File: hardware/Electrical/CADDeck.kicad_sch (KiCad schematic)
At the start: 26 parts, among them SW1 SW_Push, SW10 SW_Push, SW2 SW_Push, SW3 SW_Push, SW4 SW_Push, SW5 SW_Push, SW6 SW_Push, SW7 SW_Push, SW8 SW_Push, SW9 SW_Push, U4 49E Zoom, U5 49E Rotate, U6 TTP223

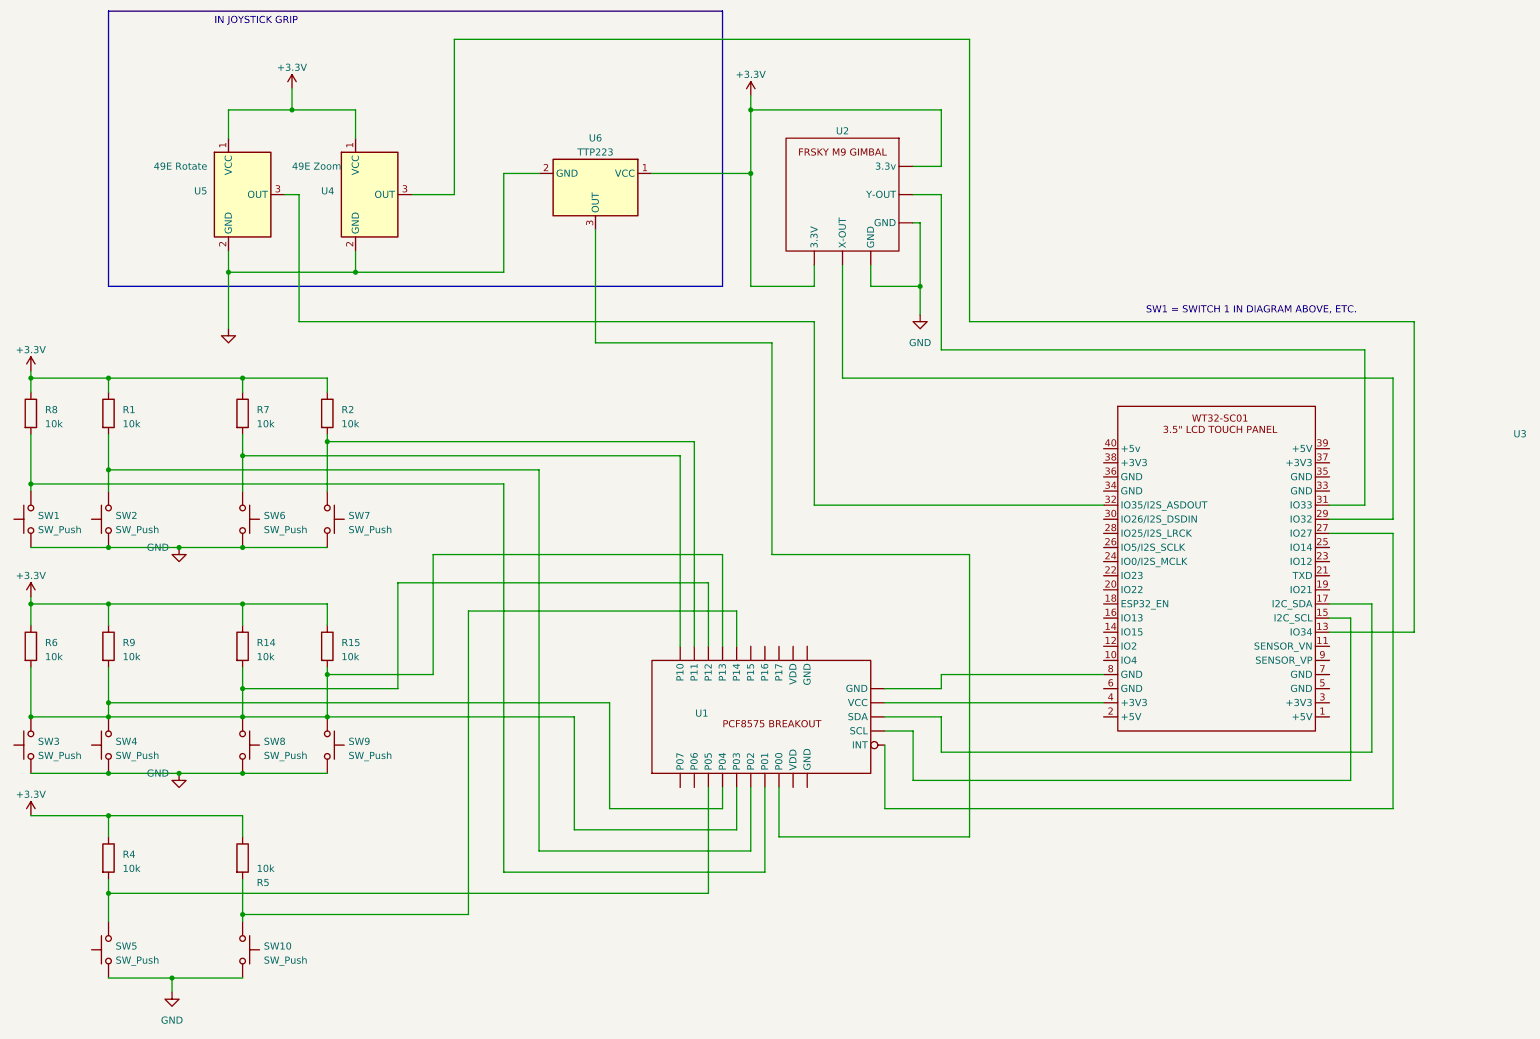
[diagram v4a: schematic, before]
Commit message: Schaltplan aktualisiert
Ist noch nicht ganz fertig um ein Board zu erstellen
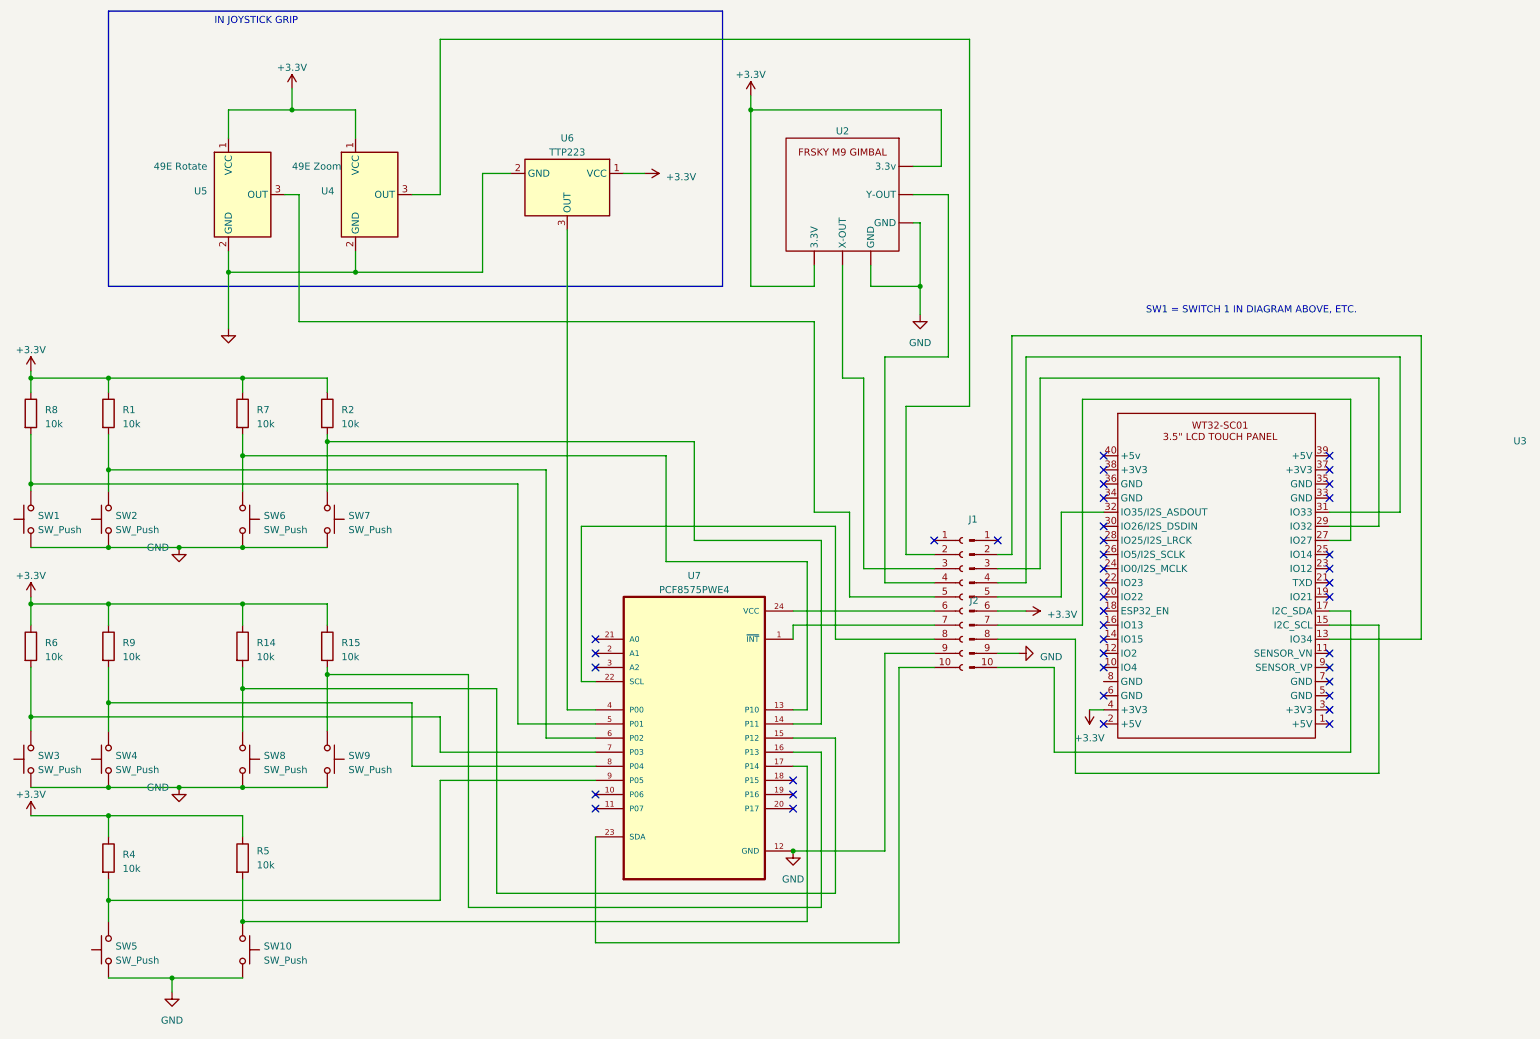
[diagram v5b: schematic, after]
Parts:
- removed U1: ~, symbol PCF8575 Breakout:PCF8575_Breakout
- added J1: Conn_01x10_Pin, Connector_JST:JST_EH_B10B-EH-A_1x10_P2.50mm_Vertical, symbol Connector:Conn_01x10_Pin
- added J2: Conn_01x10_Socket, Connector_JST:JST_EH_B10B-EH-A_1x10_P2.50mm_Vertical, symbol Connector:Conn_01x10_Socket
- added U7: PCF8575PWE4, PCF8575:SOP65P640X120-24N, symbol PCF8575PWE4:PCF8575PWE4
- R4, R5, R6, R8: footprint (none) -> Resistor_SMD:R_0805_2012Metric_Pad1.20x1.40mm_HandSolder
- SW1, SW10, SW2, SW3, SW4, SW5, SW6, SW7, SW8, SW9: footprint (none) -> Button_Switch_Keyboard:SW_Cherry_MX_1.00u_PCB
- U2: footprint (none) -> Connector_JST:JST_EH_B4B-EH-A_1x04_P2.50mm_Vertical
- U3: footprint (none) -> Connector_PinHeader_2.54mm:PinHeader_1x10_P2.54mm_Horizontal
- U4, U5, U6: footprint Package_TO_SOT_THT:TO-92_Inline -> Connector_JST:JST_EH_B3B-EH-A_1x03_P2.50mm_Vertical
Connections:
- net +3.3V: now also U3.4 (+3V3), J1.6 (Pin_6)
- net GND: now also J1.9 (Pin_9), J2.9 (Pin_9), U7.12 (GND)
- net at R7.2, SW6.1: now also U7.13 (P10)
- net at R4.2, SW5.2: now also U7.9 (P05)
- net at R1.2, SW2.2: now also U7.6 (P02)
- net at R5.2, SW10.1: now also U7.17 (P14)
- net at R2.2, SW7.1: now also U7.14 (P11)
- net at U6.3 (OUT): now also U7.4 (P00)
- net at R8.2, SW1.2: now also U7.5 (P01)
- net at U3.15 (I2C_SCL): now also J1.8 (Pin_8)
- net at U3.17 (I2C_SDA): now also J1.10 (Pin_10)
- net at U3.27 (IO27): now also J1.7 (Pin_7)
- net at U3.29 (IO32): now also J1.3 (Pin_3); no longer U2. (Y-OUT)
- net at U3.31 (IO33): now also J1.4 (Pin_4); no longer U2. (Y-OUT)
- net at U3.32 (IO35/I2S_ASDOUT): now also J1.5 (Pin_5); no longer U5.3 (OUT)
- net at U3.13 (IO34): now also J1.2 (Pin_2); no longer U4.3 (OUT)
- new net: J2.3 (Pin_3), U2. (Y-OUT)
- new net: J2.4 (Pin_4), U2. (Y-OUT)
- new net: R14.2, SW8.1, U7.15 (P12)
- new net: J2.5 (Pin_5), U5.3 (OUT)
- new net: R9.2, SW4.2, U7.8 (P04)
- new net: R15.2, SW9.1, U7.16 (P13)
- new net: R6.2, SW3.2, U7.7 (P03)
- new net: J2.2 (Pin_2), U4.3 (OUT)
- new net: J2.10 (Pin_10), U7.23 (SDA)
- new net: J2.6 (Pin_6), U7.24 (VCC)
- new net: J2.7 (Pin_7), U7.1 (~{INT})
- new net: J2.8 (Pin_8), U7.22 (SCL)
- no-connect marks 0 -> 41
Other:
- moved on the sheet: SW3, SW4, SW8, SW9, U3, U6

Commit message: Platinen Erstellung in Arbeit
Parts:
- added J3: Conn_01x05_Socket, Connector_JST:JST_EH_B5B-EH-A_1x05_P2.50mm_Vertical, symbol Connector:Conn_01x05_Socket
- added J4: Conn_01x05_Pin, symbol Connector:Conn_01x05_Pin
- added J5: Conn_01x04_Pin, symbol Connector:Conn_01x04_Pin
- added J6: Conn_01x04_Socket, Connector_JST:JST_EH_B4B-EH-A_1x04_P2.50mm_Vertical, symbol Connector:Conn_01x04_Socket
- J1: footprint Connector_JST:JST_EH_B10B-EH-A_1x10_P2.50mm_Vertical -> (none)
- U2: renamed from U3; footprint Connector_PinHeader_2.54mm:PinHeader_1x10_P2.54mm_Horizontal -> (none)
- U3: renamed from U2; footprint Connector_JST:JST_EH_B4B-EH-A_1x04_P2.50mm_Vertical -> (none)
- U4: renamed from U6; footprint Connector_JST:JST_EH_B3B-EH-A_1x03_P2.50mm_Vertical -> (none)
- U4, U5: footprint Connector_JST:JST_EH_B3B-EH-A_1x03_P2.50mm_Vertical -> (none)
- renumbered U7 to U1
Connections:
- net +3.3V: now also J3.5 (Pin_5), J6.1 (Pin_1); no longer U3. (Y-OUT), U4.1 (VCC), U4.1 (VCC), U5.1 (VCC)
- net GND: now also J3.4 (Pin_4), J4.4 (Pin_4), J6.2 (Pin_2); no longer U3. (Y-OUT)
- net at U3. (Y-OUT): now also J5.4 (Pin_4); no longer J2.3 (Pin_3)
- net at J2.4 (Pin_4): now also J6.4 (Pin_4); no longer U3. (Y-OUT)
- net at U5.3 (OUT): now also J4.1 (Pin_1); no longer J2.5 (Pin_5)
- net at U1.4 (P00): now also J3.3 (Pin_3); no longer U4.3 (OUT)
- net at J2.2 (Pin_2): now also J3.2 (Pin_2); no longer U4.3 (OUT)
- new net: J5.1 (Pin_1), U3. (Y-OUT)
- new net: J5.2 (Pin_2), U3. (Y-OUT)
- new net: J5.3 (Pin_3), U3. (Y-OUT)
- new net: J4.5 (Pin_5), U4.1 (VCC), U4.1 (VCC), U5.1 (VCC)
- new net: J2.5 (Pin_5), J3.1 (Pin_1)
- new net: J4.3 (Pin_3), U4.3 (OUT)
- new net: J4.2 (Pin_2), U4.3 (OUT)
- new net: J2.3 (Pin_3), J6.3 (Pin_3)

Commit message: Platine geroutet
aber noch nicht auf Fehler überprüft
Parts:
- renumbered J3 to J1, J4 to J2, J5 to J3, J6 to J4, J2 to J5, J1 to J6, R8 to R1, R15 to R10, R6 to R2, R1 to R3, R9 to R4, R4 to R5, R7 to R6, R14 to R7, R5 to R8, R2 to R9, SW9 to SW10, SW3 to SW2, SW2 to SW3, SW8 to SW7, SW10 to SW8, SW7 to SW9, U4 to U3, U3 to U4, U4 to U6
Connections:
- net +3.3V: now also J5.6 (Pin_6), U1.24 (VCC); no longer J6.6 (Pin_6), U2.4 (+3V3)
- new net: J6.6 (Pin_6), U2.4 (+3V3)
